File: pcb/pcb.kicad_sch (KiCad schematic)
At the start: 18 parts, among them J1 USB_C_Receptacle_USB2.0_16P, SW1 SW_Push, U1 USBLC6-2SC6, U2 XC6206PxxxMR, U3 STM32F072CBTx

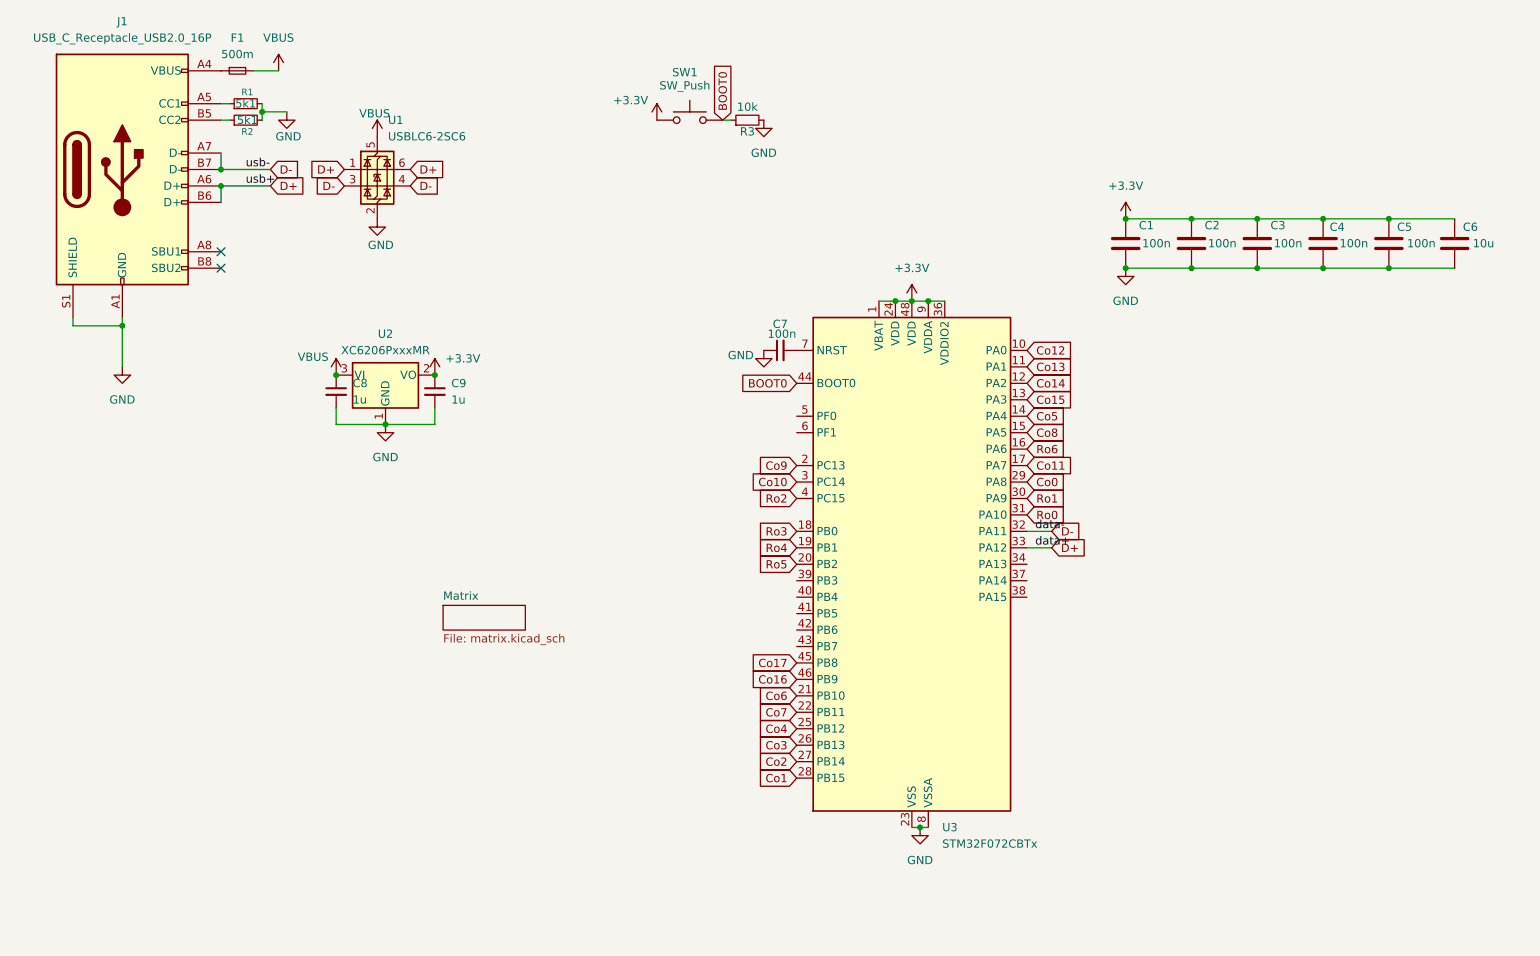
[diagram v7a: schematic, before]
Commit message: Add some LSCPCB footprints
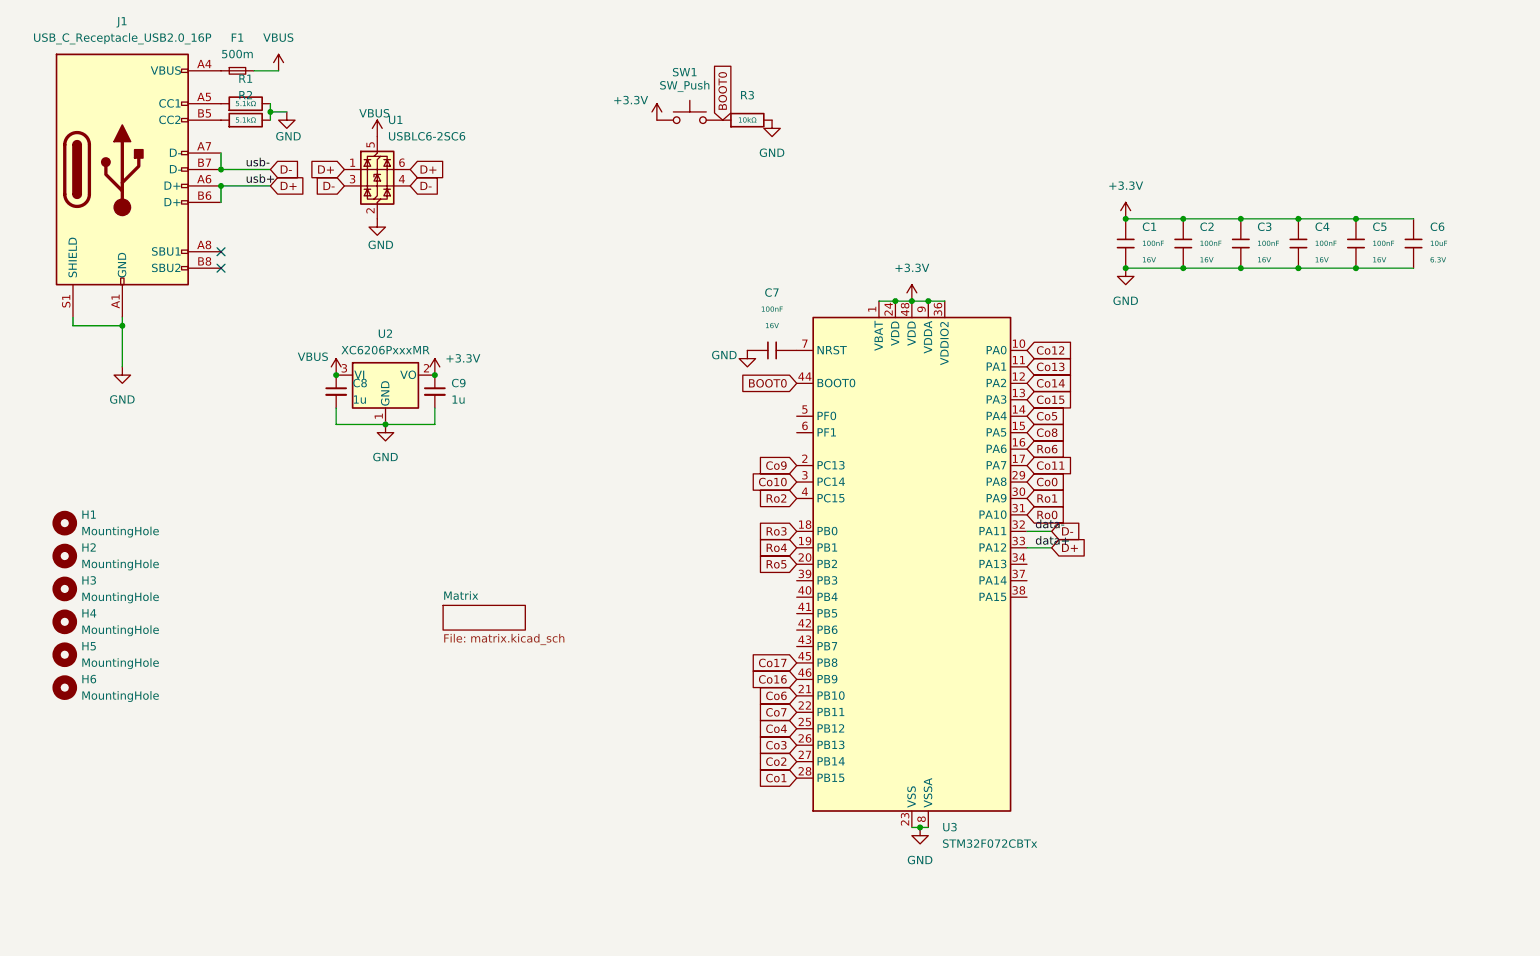
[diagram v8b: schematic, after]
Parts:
- removed C1, C2, C3, C4, C5: 100n, Capacitor_SMD:C_0402_1005Metric, symbol Device:C
- removed C6: 10u, Capacitor_SMD:C_0402_1005Metric, symbol Device:C
- removed C7: 100n, Capacitor_SMD:C_0201_0603Metric, symbol Device:C_Small
- removed R1, R2: 5k1, Resistor_SMD:R_0402_1005Metric, symbol Device:R_Small
- removed R3: 10k, Resistor_SMD:R_0402_1005Metric, symbol Device:R_Small
- added C1, C2, C3, C4, C5, C7: 100nF, PCM_JLCPCB:C_0402, symbol PCM_JLCPCB-Capacitors:0402,100nF
- added C6: 10uF, PCM_JLCPCB:C_0402, symbol PCM_JLCPCB-Capacitors:0402,10uF
- added H1, H2, H3, H4, H5, H6: MountingHole, MountingHole:MountingHole_2mm, symbol Mechanical:MountingHole
- added R1, R2: 5.1kΩ, PCM_JLCPCB:R_0402, symbol PCM_JLCPCB-Resistors:0402,5.1kΩ
- added R3: 10kΩ, PCM_JLCPCB:R_0402, symbol PCM_JLCPCB-Resistors:0402,10kΩ
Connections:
- net +3.3V: now also C1.2, C2.2, C3.2, C4.2, C5.2, C6.1
- net BOOT0: now also R3.1
- net GND: now also C1.1, C2.1, C3.1, C4.1, C5.1, C6.2, C7.1, R1.2, R2.2, R3.2
- net at J1.A5 (CC1): now also R1.1
- net at U3.7 (NRST): now also C7.2
- net at J1.B5 (CC2): now also R2.1
